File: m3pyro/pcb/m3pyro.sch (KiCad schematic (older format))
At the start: 54 parts, among them IC1 STM32F405RxTx, IC2 MCP2562, J10 WEST BOT, J11 EAST TOP, J12 EAST BOT, J9 WEST TOP, Q1 2FET3, Q2 2FET3, Q3 2FET3, Q4 2FET3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

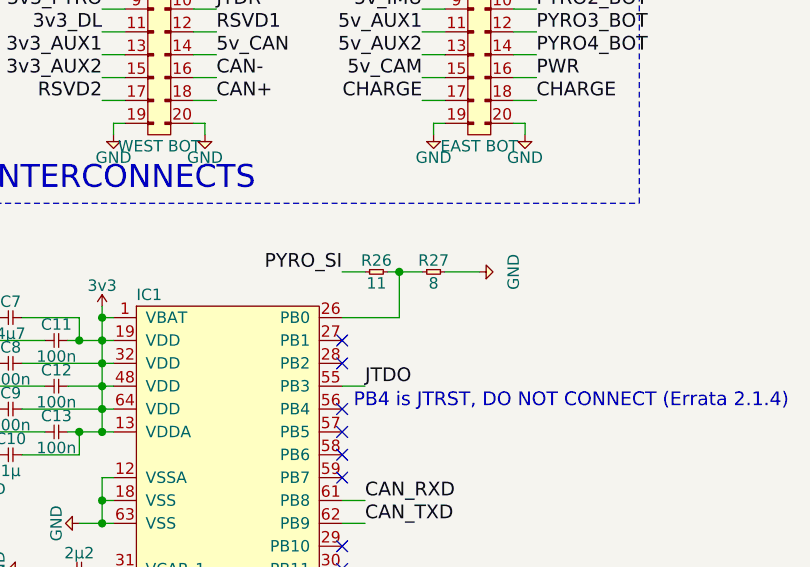
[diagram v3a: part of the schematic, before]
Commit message: add bom for m3pyro
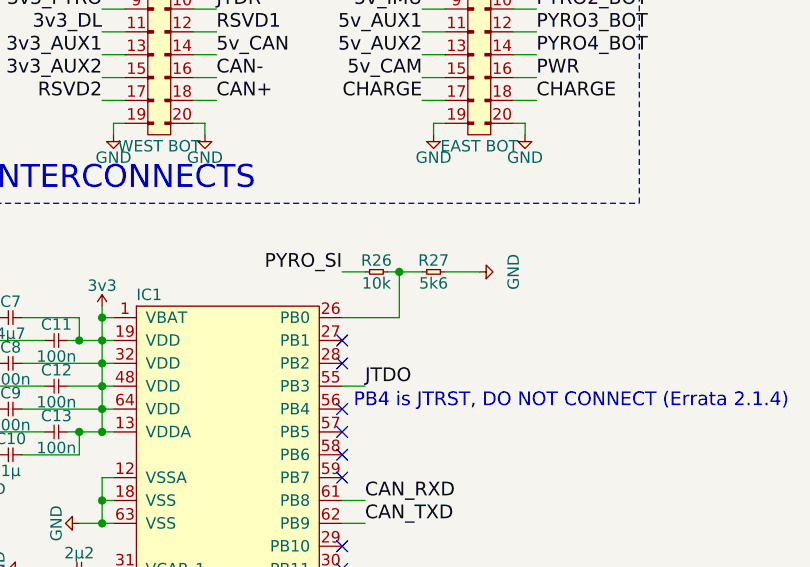
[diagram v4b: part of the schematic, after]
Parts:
- C1, C2, C3, C4: Farnell (none) -> 2496771
- D1, D2, D3, D4: Farnell (none) -> 2317565
- Q1, Q2, Q3, Q4: Farnell (none) -> 2335390
- R1, R10, R11, R12, R13, R14, R15, R16, R17, R5, R8, R9: Farnell (none) -> 2447096
- R18, R19, R20, R6: Farnell (none) -> 9239111
- R2, R3, R4, R7: Farnell (none) -> 2447120
- R26: value 11 -> 10k; Farnell (none) -> 2447096
- R27: value 8 -> 5k6; Farnell (none) -> 2502556
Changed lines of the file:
@@
 EESchema Schematic File Version 2
+LIBS:agg-kicad
+LIBS:m3pyro-cache
 LIBS:m3pyro-rescue
-LIBS:agg-kicad
 LIBS:extended pyro library
-LIBS:m3pyro-cache
 EELAYER 25 0
 EELAYER END
@@
 F 2 "agg:0402" H 1520 1590 50  0001 C CNN
 F 3 "" H 1520 1590 50  0001 C CNN
+F 4 "2447120" H 1520 1590 60  0001 C CNN "Farnell"
 	1    1520 1590
 	0    1    1    0
@@
 F 2 "agg:0402" H 2100 1940 50  0001 C CNN
 F 3 "" H 2100 1940 50  0001 C CNN
+F 4 "2317565" H 2100 1940 60  0001 C CNN "Farnell"
 	1    2100 1940
 	0    -1   -1   0
@@
 F 2 "agg:0402" H 1600 790 50  0001 C CNN
 F 3 "" H 1600 790 50  0001 C CNN
+F 4 "2447096" H 1600 790 60  0001 C CNN "Farnell"
 	1    1600 790
 	0    1    1    0
@@
 F 2 "agg:0402" H 1800 1440 50  0001 C CNN
 F 3 "" H 1800 1440 50  0001 C CNN
+F 4 "2447096" H 1800 1440 60  0001 C CNN "Farnell"
 	1    1800 1440
 	0    1    1    0
@@
 F 2 "agg:0402" H 2000 1410 50  0001 C CNN
 F 3 "" H 2000 1410 50  0001 C CNN
+F 4 "9239111" H 2000 1410 60  0001 C CNN "Farnell"
 	1    2000 1410
 	1    0    0    -1
@@
 F 2 "agg:0402" H 1900 1740 50  0001 C CNN
 F 3 "" H 1900 1740 50  0001 C CNN
+F 4 "2447096" H 1900 1740 60  0001 C CNN "Farnell"
 	1    1900 1740
 	1    0    0    -1
@@
 F 2 "agg:0402" H 2350 1790 50  0001 C CNN
 F 3 "" H 2350 1790 50  0001 C CNN
+F 4 "2496771" H 2350 1790 60  0001 C CNN "Farnell"
 	1    2350 1790
 	0    1    1    0
@@
 P 5850 3550
 F 0 "R26" H 5900 3600 50  0000 C CNN
-F 1 "11" H 5900 3500 50  0000 C CNN
+F 1 "10k" H 5900 3500 50  0000 C CNN
 F 2 "agg:0402" H 5850 3550 50  0001 C CNN
 F 3 "" H 5850 3550 50  0001 C CNN
+F 4 "2447096" H 5850 3550 60  0001 C CNN "Farnell"
 	1    5850 3550
 	1    0    0    -1
@@
 P 6100 3550
 F 0 "R27" H 6150 3600 50  0000 C CNN
-F 1 "8" H 6150 3500 50  0000 C CNN
+F 1 "5k6" H 6150 3500 50  0000 C CNN
 F 2 "agg:0402" H 6100 3550 50  0001 C CNN
 F 3 "" H 6100 3550 50  0001 C CNN
+F 4 "2502556" H 6100 3550 60  0001 C CNN "Farnell"
 	1    6100 3550
 	1    0    0    -1
@@
 F 2 "agg:0402" H 1510 3340 50  0001 C CNN
 F 3 "" H 1510 3340 50  0001 C CNN
+F 4 "2447120" H 1510 3340 60  0001 C CNN "Farnell"
 	1    1510 3340
 	0    1    1    0
@@
 F 2 "agg:0402" H 2090 3690 50  0001 C CNN
 F 3 "" H 2090 3690 50  0001 C CNN
+F 4 "2317565" H 2090 3690 60  0001 C CNN "Farnell"
 	1    2090 3690
 	0    -1   -1   0
@@
 F 2 "agg:0402" H 1590 2540 50  0001 C CNN
 F 3 "" H 1590 2540 50  0001 C CNN
+F 4 "2447096" H 1590 2540 60  0001 C CNN "Farnell"
 	1    1590 2540
 	0    1    1    0
@@
 F 2 "agg:0402" H 1790 3190 50  0001 C CNN
 F 3 "" H 1790 3190 50  0001 C CNN
+F 4 "2447096" H 1790 3190 60  0001 C CNN "Farnell"
 	1    1790 3190
 	0    1    1    0
@@
 F 2 "agg:0402" H 1990 3160 50  0001 C CNN
 F 3 "" H 1990 3160 50  0001 C CNN
+F 4 "9239111" H 1990 3160 60  0001 C CNN "Farnell"
 	1    1990 3160
 	1    0    0    -1
@@
 F 2 "agg:0402" H 1890 3490 50  0001 C CNN
 F 3 "" H 1890 3490 50  0001 C CNN
+F 4 "2447096" H 1890 3490 60  0001 C CNN "Farnell"
 	1    1890 3490
 	1    0    0    -1
@@
 F 2 "agg:0402" H 2340 3540 50  0001 C CNN
 F 3 "" H 2340 3540 50  0001 C CNN
+F 4 "2496771" H 2340 3540 60  0001 C CNN "Farnell"
 	1    2340 3540
 	0    1    1    0
@@
 F 2 "agg:0402" H 1510 5080 50  0001 C CNN
 F 3 "" H 1510 5080 50  0001 C CNN
+F 4 "2447120" H 1510 5080 60  0001 C CNN "Farnell"
 	1    1510 5080
 	0    1    1    0
@@
 F 2 "agg:0402" H 2090 5430 50  0001 C CNN
 F 3 "" H 2090 5430 50  0001 C CNN
+F 4 "2317565" H 2090 5430 60  0001 C CNN "Farnell"
 	1    2090 5430
 	0    -1   -1   0
@@
 F 2 "agg:0402" H 1590 4280 50  0001 C CNN
 F 3 "" H 1590 4280 50  0001 C CNN
+F 4 "2447096" H 1590 4280 60  0001 C CNN "Farnell"
 	1    1590 4280
 	0    1    1    0
@@
 F 2 "agg:0402" H 1790 4930 50  0001 C CNN
 F 3 "" H 1790 4930 50  0001 C CNN
+F 4 "2447096" H 1790 4930 60  0001 C CNN "Farnell"
 	1    1790 4930
 	0    1    1    0
@@
 F 2 "agg:0402" H 1990 4900 50  0001 C CNN
 F 3 "" H 1990 4900 50  0001 C CNN
+F 4 "9239111" H 1990 4900 60  0001 C CNN "Farnell"
 	1    1990 4900
 	1    0    0    -1
@@
 F 2 "agg:0402" H 1890 5230 50  0001 C CNN
 F 3 "" H 1890 5230 50  0001 C CNN
+F 4 "2447096" H 1890 5230 60  0001 C CNN "Farnell"
 	1    1890 5230
 	1    0    0    -1
@@
 F 2 "agg:0402" H 2340 5280 50  0001 C CNN
 F 3 "" H 2340 5280 50  0001 C CNN
+F 4 "2496771" H 2340 5280 60  0001 C CNN "Farnell"
 	1    2340 5280
 	0    1    1    0
@@
 F 2 "agg:0402" H 1520 6780 50  0001 C CNN
 F 3 "" H 1520 6780 50  0001 C CNN
+F 4 "2447120" H 1520 6780 60  0001 C CNN "Farnell"
 	1    1520 6780
 	0    1    1    0
@@
 F 2 "agg:0402" H 2100 7130 50  0001 C CNN
 F 3 "" H 2100 7130 50  0001 C CNN
+F 4 "2317565" H 2100 7130 60  0001 C CNN "Farnell"
 	1    2100 7130
 	0    -1   -1   0
@@
 F 2 "agg:0402" H 1600 5980 50  0001 C CNN
 F 3 "" H 1600 5980 50  0001 C CNN
+F 4 "2447096" H 1600 5980 60  0001 C CNN "Farnell"
 	1    1600 5980
 	0    1    1    0
@@
 F 2 "agg:0402" H 1800 6630 50  0001 C CNN
 F 3 "" H 1800 6630 50  0001 C CNN
+F 4 "2447096" H 1800 6630 60  0001 C CNN "Farnell"
 	1    1800 6630
 	0    1    1    0
@@
 F 2 "agg:0402" H 2000 6600 50  0001 C CNN
 F 3 "" H 2000 6600 50  0001 C CNN
+F 4 "9239111" H 2000 6600 60  0001 C CNN "Farnell"
 	1    2000 6600
 	1    0    0    -1
@@
 F 2 "agg:0402" H 1900 6930 50  0001 C CNN
 F 3 "" H 1900 6930 50  0001 C CNN
+F 4 "2447096" H 1900 6930 60  0001 C CNN "Farnell"
 	1    1900 6930
 	1    0    0    -1
@@
 F 2 "agg:0402" H 2350 6980 50  0001 C CNN
 F 3 "" H 2350 6980 50  0001 C CNN
+F 4 "2496771" H 2350 6980 60  0001 C CNN "Farnell"
 	1    2350 6980
 	0    1    1    0
@@
 F 2 "m3pyro:PowerPAK-SC-70-6-DUAL" H 1100 5720 50  0001 C CNN
 F 3 "" H 1100 5720 50  0001 C CNN
+F 4 "2335390" H 1500 5920 60  0001 C CNN "Farnell"
 	1    1500 5920
 	0    -1   -1   0
@@
 F 2 "m3pyro:PowerPAK-SC-70-6-DUAL" H 1090 4020 50  0001 C CNN
 F 3 "" H 1090 4020 50  0001 C CNN
+F 4 "2335390" H 1490 4220 60  0001 C CNN "Farnell"
 	1    1490 4220
 	0    -1   -1   0
@@
 F 2 "m3pyro:PowerPAK-SC-70-6-DUAL" H 1090 2280 50  0001 C CNN
 F 3 "" H 1090 2280 50  0001 C CNN
+F 4 "2335390" H 1490 2480 60  0001 C CNN "Farnell"
 	1    1490 2480
 	0    -1   -1   0
@@
 F 2 "m3pyro:PowerPAK-SC-70-6-DUAL" H 1100 530 50  0001 C CNN
 F 3 "" H 1100 530 50  0001 C CNN
+F 4 "2335390" H 1500 730 60  0001 C CNN "Farnell"
 	1    1500 730
 	0    -1   -1   0
